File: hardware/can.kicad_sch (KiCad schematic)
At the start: 15 parts, among them U5 ADM3057ExRW

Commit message: Fixes after review
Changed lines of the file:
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@@
+		)
+	)
+	(wire
+		(pts
+			(xy 74.93 121.92) (xy 82.55 121.92)
+		)
+		(stroke
+			(width 0)
+			(type default)
+		)
+	)
+	(wire
+		(pts
+			(xy 82.55 105.41) (xy 82.55 113.03)
+		)
+		(stroke
+			(width 0)
+			(type default)
+		)
+	)
+	(wire
+		(pts
+			(xy 133.35 76.2) (xy 133.35 69.85)
+		)
+		(stroke
+			(width 0)
+			(type default)
+		)
+	)
+	(wire
+		(pts
+			(xy 140.97 99.06) (xy 144.78 99.06)
+		)
+		(stroke
+			(width 0)
+			(type default)
+		)
+	)
+	(wire
+		(pts
+			(xy 104.14 76.2) (xy 118.11 76.2)
+		)
+		(stroke
+			(width 0)
+			(type default)
+		)
+	)
+	(wire
+		(pts
+			(xy 130.81 111.76) (xy 130.81 114.3)
+		)
+		(stroke
+			(width 0)
+			(type default)
+		)
+	)
+	(wire
+		(pts
+			(xy 68.58 107.95) (xy 76.2 107.95)
+		)
+		(stroke
+			(width 0)
+			(type default)
+		)
+	)
+	(wire
+		(pts
+			(xy 100.33 100.33) (xy 110.49 100.33)
+		)
+		(stroke
+			(width 0)
+			(type default)
+		)
+	)
+	(wire
+		(pts
+			(xy 137.16 57.15) (xy 143.51 57.15)
+		)
+		(stroke
+			(width 0)
+			(type default)
+		)
+	)
+	(wire
+		(pts
+			(xy 129.54 57.15) (xy 132.08 57.15)
+		)
+		(stroke
+			(width 0)
+			(type default)
 		)
 	)
 	(polyline
 		(pts
-			(xy 125.73 37.846) (xy 125.476 136.906)
-		)
-		(stroke
-			(width 0)
-			(type dot)
-		)
-	)
-	(wire
-		(pts
-			(xy 74.93 121.92) (xy 82.55 121.92)
-		)
-		(stroke
-			(width 0)
-			(type default)
-		)
-	)
-	(wire
-		(pts
-			(xy 82.55 105.41) (xy 82.55 113.03)
-		)
-		(stroke
-			(width 0)
-			(type default)
-		)
-	)
-	(wire
-		(pts
-			(xy 133.35 76.2) (xy 133.35 69.85)
-		)
-		(stroke
-			(width 0)
-			(type default)
-		)
-	)
-	(wire
-		(pts
-			(xy 140.97 99.06) (xy 144.78 99.06)
-		)
-		(stroke
-			(width 0)
-			(type default)
-		)
-	)
-	(wire
-		(pts
-			(xy 104.14 76.2) (xy 118.11 76.2)
-		)
-		(stroke
-			(width 0)
-			(type default)
-		)
-	)
-	(wire
-		(pts
-			(xy 130.81 111.76) (xy 130.81 114.3)
-		)
-		(stroke
-			(width 0)
-			(type default)
-		)
-	)
-	(wire
-		(pts
-			(xy 68.58 107.95) (xy 76.2 107.95)
-		)
-		(stroke
-			(width 0)
-			(type default)
-		)
-	)
-	(wire
-		(pts
-			(xy 100.33 100.33) (xy 110.49 100.33)
-		)
-		(stroke
-			(width 0)
-			(type default)
-		)
-	)
-	(wire
-		(pts
-			(xy 137.16 57.15) (xy 143.51 57.15)
-		)
-		(stroke
-			(width 0)
-			(type default)
-		)
-	)
-	(wire
-		(pts
-			(xy 129.54 57.15) (xy 132.08 57.15)
-		)
-		(stroke
-			(width 0)
-			(type default)
+			(xy 126.238 12.192) (xy 126.238 197.866)
+		)
+		(stroke
+			(width 0.381)
+			(type solid)
+			(color 194 0 0 1)
 		)
 	)
@@
 		)
 	)
+	(polyline
+		(pts
+			(xy 125.222 12.192) (xy 125.222 197.866)
+		)
+		(stroke
+			(width 0.381)
+			(type solid)
+			(color 194 0 0 1)
+		)
+	)

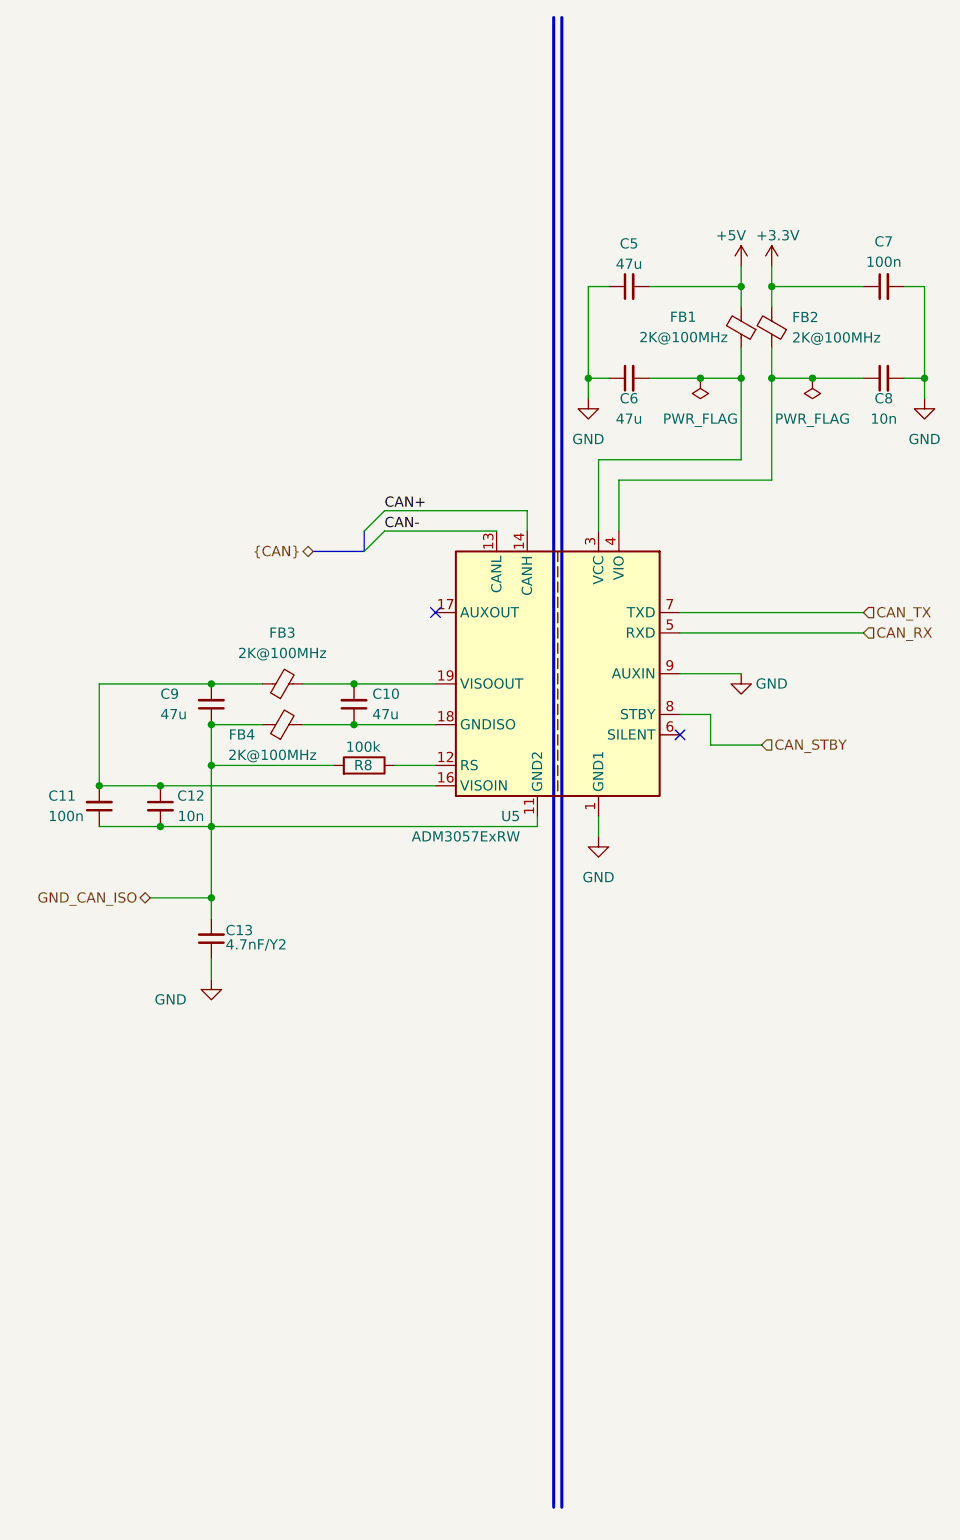
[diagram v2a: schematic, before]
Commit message: Fixes after review and mouser links for most components added
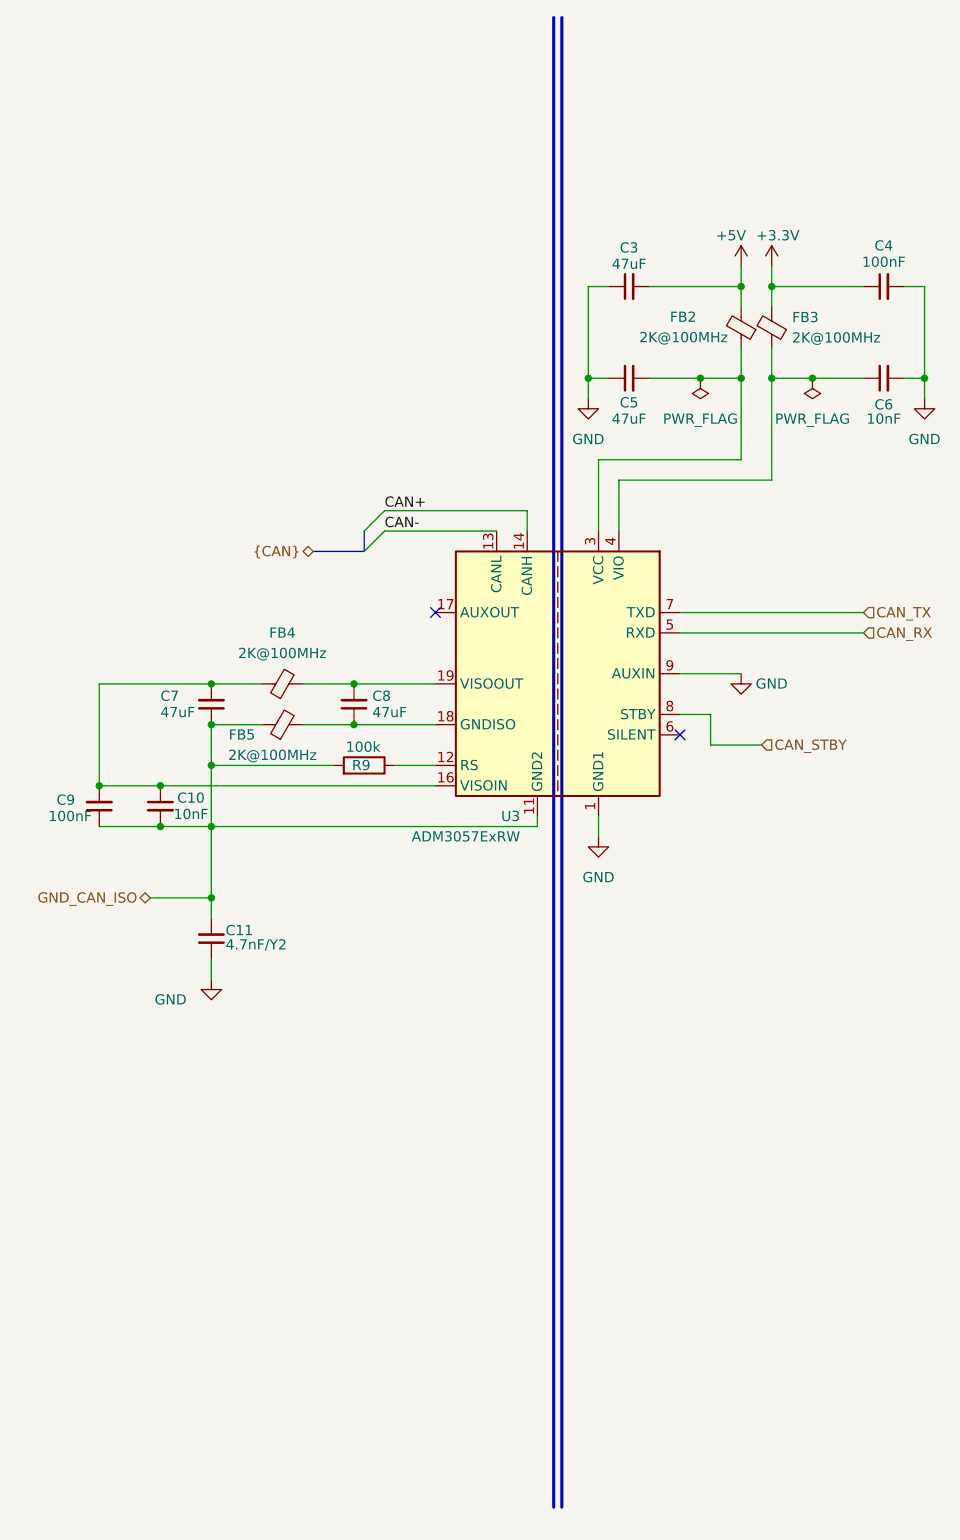
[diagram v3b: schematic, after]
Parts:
- C10: renamed from C12; value 10n -> 10nF; Mouser https://www.mouser.pl/ProductDetail/KEMET/C0603C103J5RACAUT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 -> https://www.mouser.pl/ProductDetail/Murata-Electronics/GCM1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
- C3: renamed from C5; value 47u -> 47uF
- C4: renamed from C7; value 100n -> 100nF
- C5: renamed from C6; value 47u -> 47uF
- C6: renamed from C8; value 10n -> 10nF; Mouser https://www.mouser.pl/ProductDetail/KEMET/C0603C103J5RACAUT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 -> https://www.mouser.pl/ProductDetail/Murata-Electronics/GCM1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
- C7: renamed from C9; value 47u -> 47uF
- C8: renamed from C10; value 47u -> 47uF
- C9: renamed from C11; value 100n -> 100nF
- R9: renamed from R8; Mouser https://www.mouser.pl/ProductDetail/Bourns/CRT0603-FZ-1003E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 -> https://www.mouser.pl/ProductDetail/KOA-Speer/RK73B1JTTD104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
- renumbered C13 to C11, FB1 to FB2, FB2 to FB3, FB3 to FB4, FB4 to FB5, U5 to U3

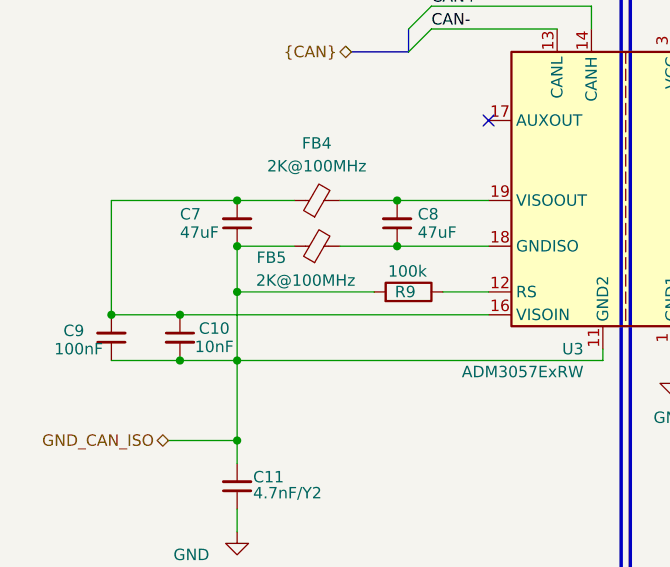
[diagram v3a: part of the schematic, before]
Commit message: changed some elements on shematic
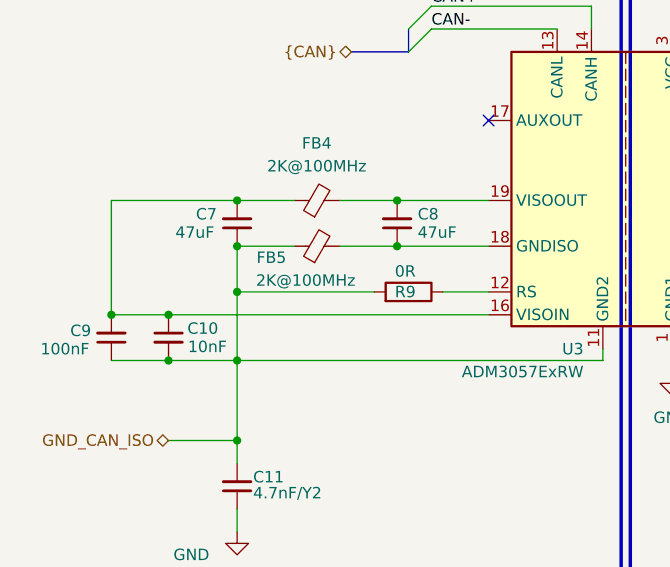
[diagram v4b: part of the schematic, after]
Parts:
- R9: value 100k -> 0R; Manufacturer_Part_Number CRT0603-FZ-1003ELF -> (none); Mouser https://www.mouser.pl/ProductDetail/KOA-Speer/RK73B1JTTD104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 -> https://www.mouser.pl/ProductDetail/YAGEO/AC0603FR-070RL?qs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; Mouser No 652-CRT0603FZ1003ELF -> (none)
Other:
- moved on the sheet: C10

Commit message: 3D models, optocoupler added, pcb settings and components placing
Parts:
- C11: footprint Samacsys:CAPC5728X280N -> samacsys:CAPC5728X280N

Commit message: Finished routing
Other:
- moved on the sheet: C11
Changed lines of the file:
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@@
 	)
 	(junction
+		(at 82.55 125.73)
+		(diameter 0)
+		(color 0 0 0 0)
+	)
+	(junction
 		(at 100.33 95.25)
 		(diameter 0)
@@
 	)
 	(junction
-		(at 82.55 121.92)
-		(diameter 0)
-		(color 0 0 0 0)
-	)
-	(junction
 		(at 74.93 113.03)
 		(diameter 0)
@@
 	(wire
 		(pts
+			(xy 82.55 113.03) (xy 82.55 125.73)
+		)
+		(stroke
+			(width 0)
+			(type default)
+		)
+	)
+	(wire
+		(pts
 			(xy 123.19 113.03) (xy 123.19 111.76)
 		)
@@
 	(wire
 		(pts
-			(xy 82.55 129.54) (xy 82.55 132.08)
+			(xy 128.27 125.73) (xy 130.81 125.73)
 		)
 		(stroke
@@
 	(wire
 		(pts
-			(xy 74.93 121.92) (xy 82.55 121.92)
+			(xy 74.93 125.73) (xy 82.55 125.73)
 		)
 		(stroke
@@
 		)
 	)
+	(polyline
+		(pts
+			(xy 126.238 127.762) (xy 126.238 199.898)
+		)
+		(stroke
+			(width 0.127)
+			(type solid)
+			(color 194 0 0 1)
+		)
+	)
 	(wire
 		(pts
@@
 	(polyline
 		(pts
-			(xy 126.238 12.192) (xy 126.238 197.866)
+			(xy 126.238 12.192) (xy 126.238 123.698)
 		)
 		(stroke
-			(width 0.381)
+			(width 0.127)
 			(type solid)
 			(color 194 0 0 1)
@@
 		)
 	)
-	(wire
+	(polyline
 		(pts
-			(xy 171.45 45.72) (xy 171.45 57.15)
+			(xy 125.222 127.762) (xy 125.222 199.898)
 		)
 		(stroke
-			(width 0)
-			(type default)
+			(width 0.127)
+			(type solid)
+			(color 194 0 0 1)
 		)
 	)
 	(wire
 		(pts
-			(xy 93.98 95.25) (xy 100.33 95.25)
+			(xy 171.45 45.72) (xy 171.45 57.15)
 		)
 		(stroke
@@
 	(wire
 		(pts
-			(xy 82.55 124.46) (xy 82.55 121.92)
+			(xy 93.98 95.25) (xy 100.33 95.25)
 		)
 		(stroke
@@
 	(wire
 		(pts
-			(xy 82.55 113.03) (xy 82.55 121.92)
-		)
-		(stroke
-			(width 0)
-			(type default)
-		)
-	)
-	(wire
-		(pts
 			(xy 171.45 59.69) (xy 171.45 57.15)
 		)
@@
 	(wire
 		(pts
+			(xy 82.55 125.73) (xy 123.19 125.73)
+		)
+		(stroke
+			(width 0)
+			(type default)
+		)
+	)
+	(wire
+		(pts
 			(xy 93.98 100.33) (xy 100.33 100.33)
 		)
@@
 	(polyline
 		(pts
-			(xy 125.222 12.192) (xy 125.222 197.866)
+			(xy 125.222 12.192) (xy 125.222 123.698)
 		)
 		(stroke
-			(width 0.381)
+			(width 0.127)
 			(type solid)
 			(color 194 0 0 1)
@@
 	(hierarchical_label "GND_CAN_ISO"
 		(shape bidirectional)
-		(at 74.93 121.92 180)
+		(at 74.93 125.73 180)
 		(effects
 			(font
@@
 	(symbol
 		(lib_id "power:GND")
-		(at 82.55 132.08 0)
+		(at 130.81 125.73 90)
 		(unit 1)
 		(body_style 1)
@@
 		(dnp no)
 		(property "Reference" "#PWR055"
-			(at 82.55 138.43 0)
+			(at 137.16 125.73 0)
 			(hide yes)
 			(show_name no)
@@
 		)
 		(property "Value" "GND"
-			(at 77.47 134.62 0)
+			(at 133.35 130.81 0)
 			(show_name no)
 			(do_not_autoplace no)
@@
 		)
 		(property "Footprint" ""
-			(at 82.55 132.08 0)
+			(at 130.81 125.73 0)
 			(hide yes)
 			(show_name no)
@@
 		)
 		(property "Datasheet" ""
-			(at 82.55 132.08 0)
+			(at 130.81 125.73 0)
 			(hide yes)
 			(show_name no)
@@
 		)
 		(property "Description" "Power symbol creates a global label with name \"GND\" , ground"
-			(at 82.55 132.08 0)
+			(at 130.81 125.73 0)
 			(hide yes)
 			(show_name no)
@@
 	(symbol
 		(lib_id "Device:C_Small")
-		(at 82.55 127 180)
+		(at 125.73 125.73 270)
 		(unit 1)
 		(body_style 1)
@@
 		(dnp no)
 		(property "Reference" "C11"
-			(at 84.328 125.984 0)
+			(at 123.952 121.666 90)
 			(show_name no)
 			(do_not_autoplace no)
@@
 		)
 		(property "Value" "4.7nF/Y2"
-			(at 84.328 127.762 0)
+			(at 135.89 122.936 90)
 			(show_name no)
 			(do_not_autoplace no)
@@
 		)
 		(property "Footprint" "samacsys:CAPC5728X280N"
-			(at 82.55 127 0)
+			(at 125.73 125.73 0)
 			(hide yes)
 			(show_name no)
@@
 		)
 		(property "Datasheet" "https://4donline.ihs.com/images/VipMasterIC/IC/WATC/WATC-S-A0011771687/WATC-S-A0011771687-1.pdf?hkey=CECEF36DEECDED6468708AAF2E19C0C6"
-			(at 82.55 127 0)
+			(at 125.73 125.73 0)
 			(hide yes)
 			(show_name no)
@@
 		)
 		(property "Description" "Safety Capacitors 2211 MLCC X7R 2200 pF , \\'+/- 10% 5K V T&R SAF"
-			(at 82.55 127 0)
+			(at 125.73 125.73 0)
 			(hide yes)
 			(show_name no)
@@
 		)
 		(property "Mouser" "https://www.mouser.pl/ProductDetail/Walsin/S252B222K502CT?qs=wUXugUrL1qx2Bha0j7hz5g%3D%3D"
-			(at 82.55 127 0)
+			(at 125.73 125.73 0)
 			(hide yes)
 			(show_name no)
@@
 		)
 		(property "Mouser No" "791-S252B222K502CT"
-			(at 82.55 127 0)
+			(at 125.73 125.73 0)
 			(hide yes)
 			(show_name no)
@@
 		)
 		(property "Manufacturer_Part_Number" "S252B222K502CT"
-			(at 82.55 127 0)
+			(at 125.73 125.73 0)
 			(hide yes)
 			(show_name no)
@@
 		)
 		(property "Author" ""
-			(at 82.55 127 0)
+			(at 125.73 125.73 0)
 			(hide yes)
 			(show_name no)
@@
 		)
 		(property "License" ""
-			(at 82.55 127 0)
+			(at 125.73 125.73 0)
 			(hide yes)
 			(show_name no)
@@
 		)
 		(property "MPN" ""
-			(at 82.55 127 0)
+			(at 125.73 125.73 0)
 			(hide yes)
 			(show_name no)
@@
 		)
 		(property "Manufacturer" ""
-			(at 82.55 127 0)
+			(at 125.73 125.73 0)
 			(hide yes)
 			(show_name no)
@@
 		)
 		(property "Sim.Device" ""
-			(at 82.55 127 0)
+			(at 125.73 125.73 0)
 			(hide yes)
 			(show_name no)
@@
 		)
 		(property "Sim.Type" ""
-			(at 82.55 127 0)
+			(at 125.73 125.73 0)
 			(hide yes)
 			(show_name no)

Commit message: Some smaller fixes and final aesthetic changes
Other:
- company: Author: -> Author: Kacper Pawlak
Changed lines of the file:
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@@
 	(paper "A4")
 	(title_block
-		(company "Author:")
+		(company "Author: Kacper Pawlak")
+		(comment 1 "Reviewer: Piotr Lesicki")
 	)
 	(junction

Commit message: Updated BOM
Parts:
- C10, C6: Manufacturer_Part_Number C0603C103J5RACAUTO -> (none); Mouser No 80-C0603C103J5RAUTO -> 81-GCM188R71H103KA7J
- C11: Manufacturer_Part_Number S252B222K502CT -> (none)
- C3, C5, C7, C8: Manufacturer_Part_Number GRM21BR61A476ME15L -> (none)
- C4, C9: Manufacturer_Part_Number C0603C104M4RACAUTO -> (none)
- FB2, FB3, FB4, FB5: Manufacturer_Part_Number 2508052027Y1 -> (none)
- R9: Mouser No (none) -> 603-AC0603FR-070RL
- U3: Manufacturer_Part_Number ADM3057EBRWZ -> (none)
